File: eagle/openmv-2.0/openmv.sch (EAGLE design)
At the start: 46 parts, among them U1 OV9650, U10 BEAD, U4 STM32F407LQFP100, X2 USB-MICROB, Y1 12Mhz

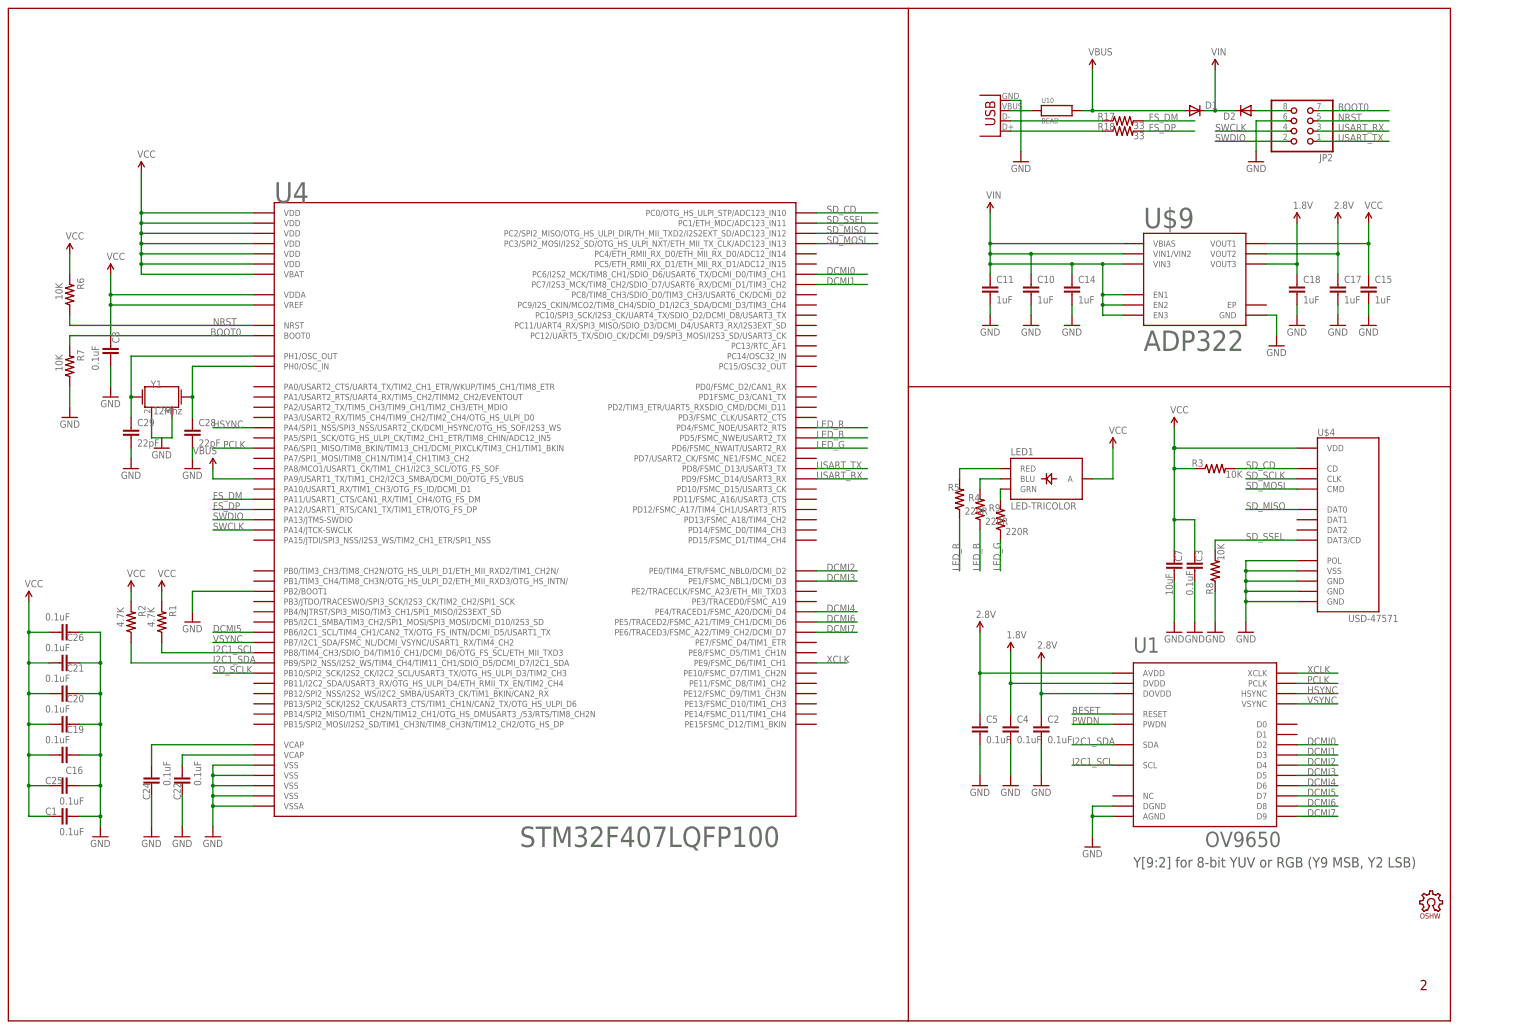
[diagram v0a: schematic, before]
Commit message: Add test points to breakout SPI3
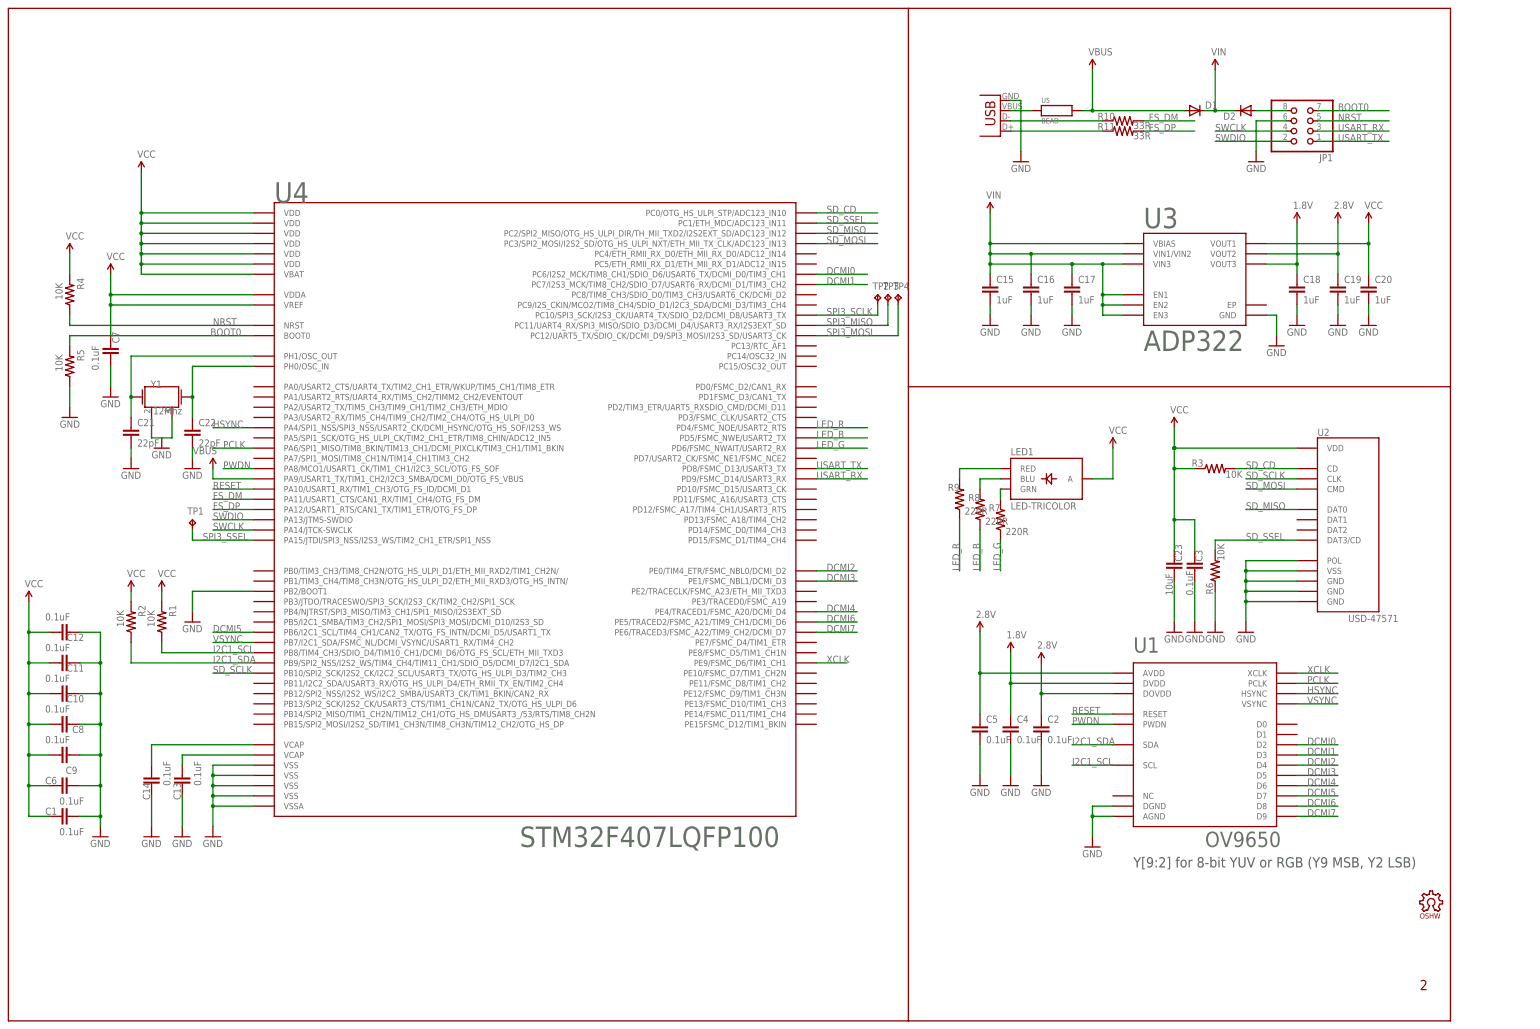
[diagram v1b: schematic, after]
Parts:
- removed C24: 0.1uF, sfe:CAP0402-CAP
- removed C28, C29: 22pF, sfe:CAP0402-CAP
- added C13, C9: 0.1uF, sfe:CAP0402-CAP
- added C23: 10uF, sfe:CAP0805
- added TP1, TP2, TP3, TP4: TPTP10R, testpad:TPTP10R
- C10, C11, C14: value 1uF -> 0.1uF
- C16, C19, C20: value 0.1uF -> 1uF
- C21, C22: value 0.1uF -> 22pF
- C7: value 10uF -> 0.1uF; device sfe:CAP0805 -> sfe:CAP0402-CAP
- R1, R2: value 4.7K -> 10K
- R10, R11: value 33 -> 33R
- R4, R5: value 220R -> 10K
- R7, R8: value 10K -> 220R
- renumbered C25 to C6, C26 to C12, JP2 to JP1, R17 to R10, R18 to R11, U$4 to U2, U$9 to U3, U10 to U5, X2 to X1
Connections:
- new net SPI3_MISO: TP3.TP, U4.PC11/UART4_RX/SPI3_MISO/SDIO_D3/DCMI_D4/USART3_RX/I2S3EXT_SD
- new net SPI3_MOSI: TP4.TP, U4.PC12/UART5_TX/SDIO_CK/DCMI_D9/SPI3_MOSI/I2S3_SD/USART3_CK
- new net SPI3_SCLK: TP2.TP, U4.PC10/SPI3_SCK/I2S3_CK/UART4_TX/SDIO_D2/DCMI_D8/USART3_TX
- new net SPI3_SSEL: TP1.TP, U4.PA15/JTDI/SPI3_NSS/I2S3_WS/TIM2_CH1_ETR/SPI1_NSS
- net 2.8V: now also C19.1; no longer C17.1
- net BOOT0: now also R5.2; no longer R7.2
- net GND: now also C13.2, C16.2, C23.2, C7.1, C8.2, C9.1, R5.1, R6.1; no longer C16.1, C24.2, C28.2, C29.2, C7.2, C8.1, R7.1, R8.1
- net LED_B: now also R8.1; no longer R4.1
- net LED_G: now also R7.1; no longer R9.1
- net LED_R: now also R9.1; no longer R5.1
- net N$10: now also C22.1; no longer C28.1
- net N$16: now also R9.2; no longer R5.2
- net N$6: now also R7.2; no longer R9.2
- net N$7: now also R8.2; no longer R4.2
- net N$9: now also C21.1; no longer C29.1
- net NRST: now also R4.1; no longer R6.1
- net PWDN: now also U4.PA8/MCO1/USART1_CK/TIM1_CH1/I2C3_SCL/OTG_FS_SOF
- net RESET: now also U4.PA10/USART1_RX/TIM1_CH3/OTG_FS_ID/DCMI_D1
- net SD_SSEL: now also R6.2; no longer R8.2
- net VCAP1: now also C14.1; no longer C24.1
- net VCAP2: now also C13.1; no longer C22.1
- net VCC: now also C10.1, C11.1, C23.1, C7.2, C8.1, C9.2, R4.2; no longer C15.1, C16.2, C19.1, C21.1, C7.1, C8.2, R6.2
- net VIN: now also C15.1, C16.1, C17.1; no longer C10.1, C11.1, C14.1
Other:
- moved on the sheet: C10, C11, C14, C15, C16, C17, C19, C20, C21, C22, C7, C8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
